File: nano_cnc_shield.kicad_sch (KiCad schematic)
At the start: 8 parts, among them Q1 IRFZ44N, U1 L7805

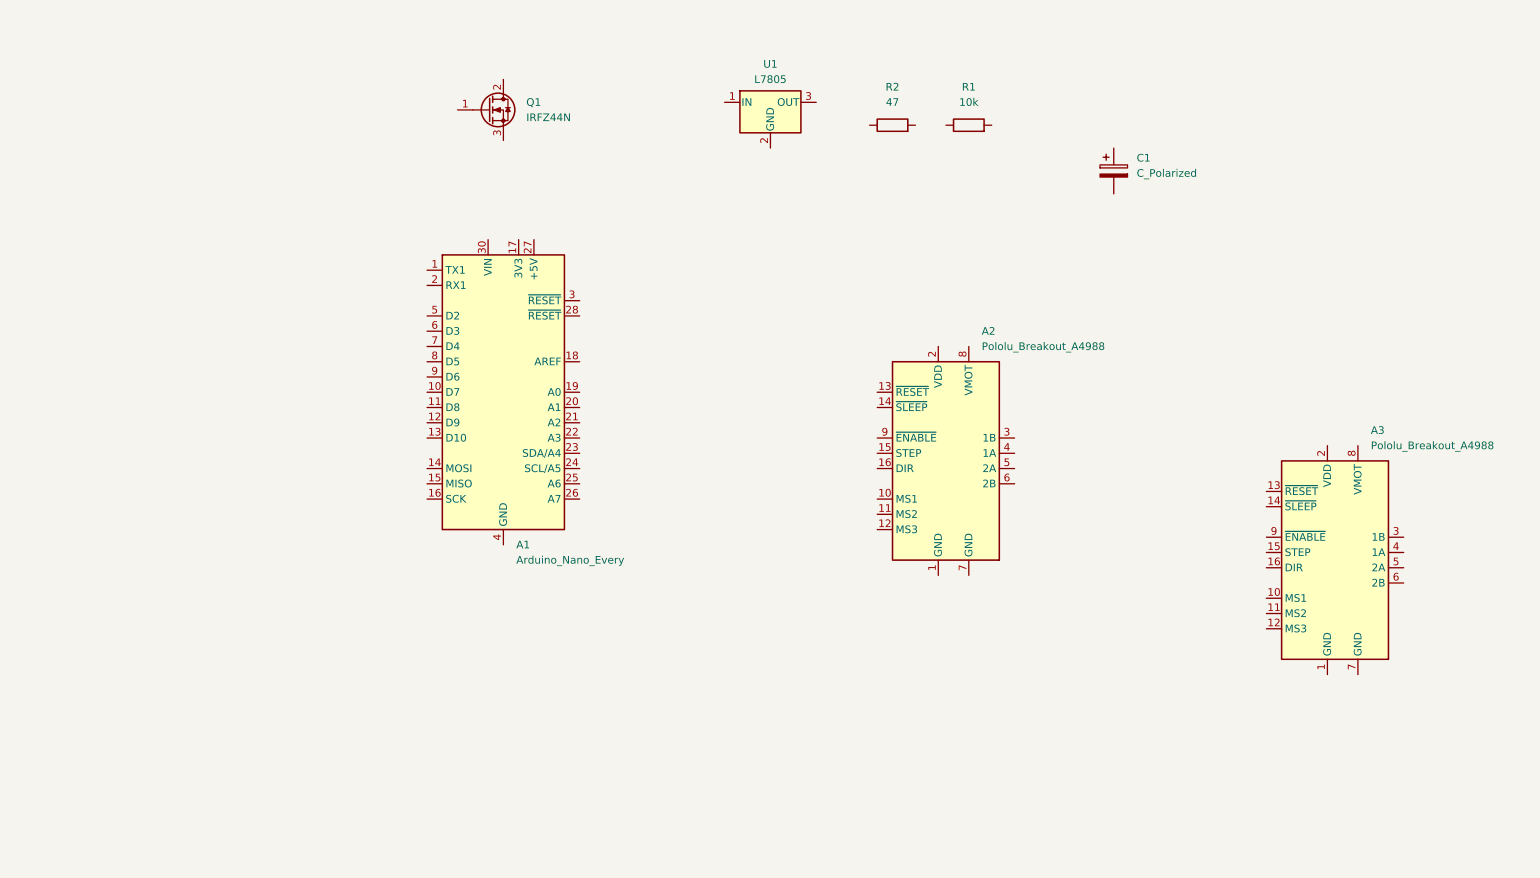
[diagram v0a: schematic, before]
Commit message: add complimentary components
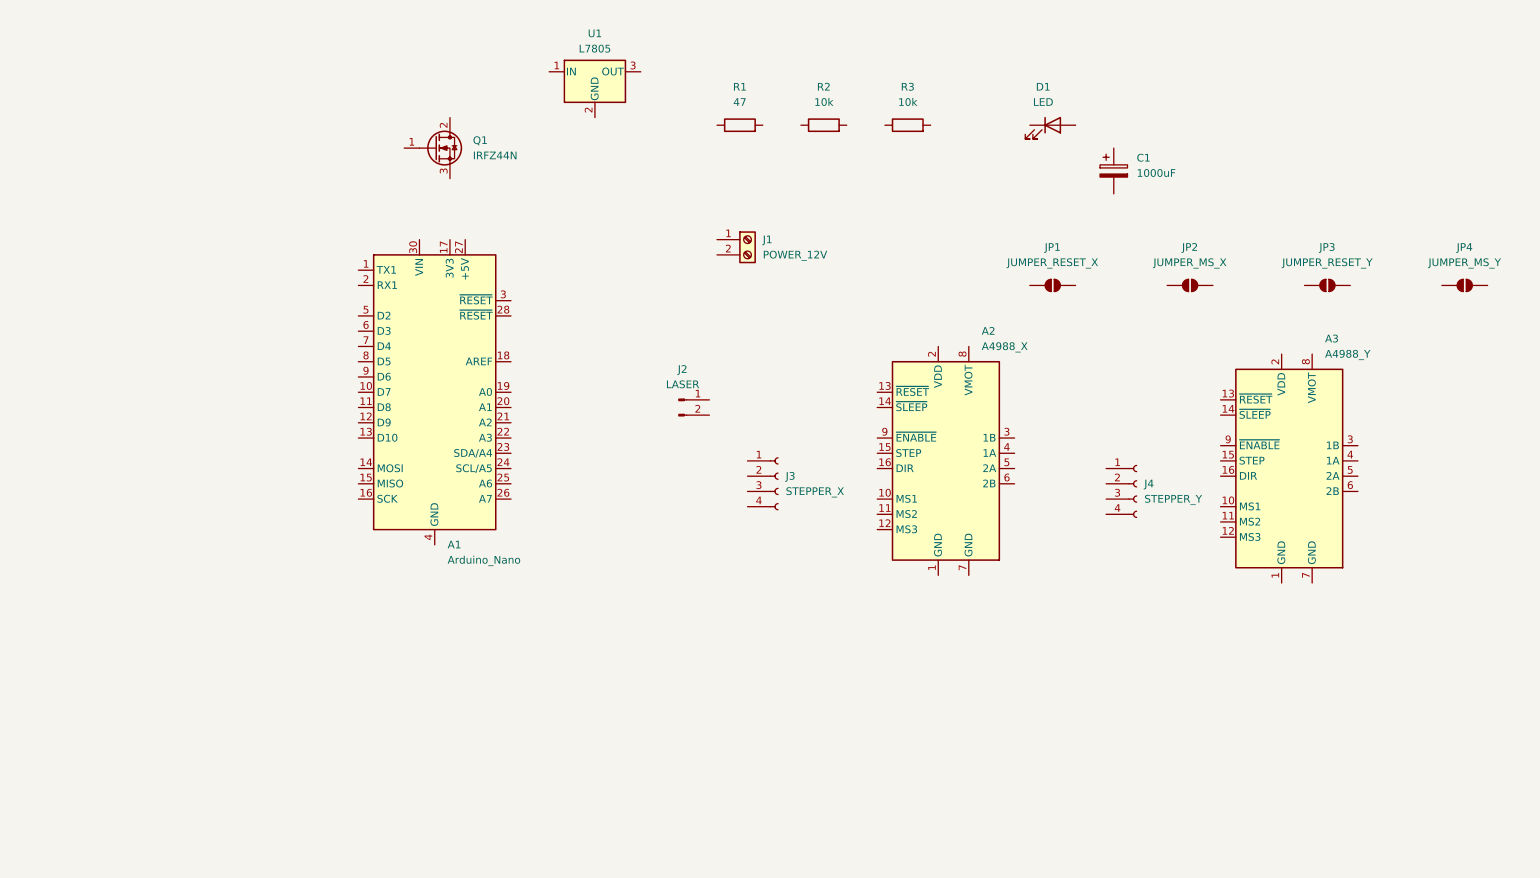
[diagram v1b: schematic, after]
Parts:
- added D1: LED, LED_THT:LED_D3.0mm, symbol Device:LED
- added J1: POWER_12V, TerminalBlock_RND:TerminalBlock_RND_205-00045_1x02_P5.00mm_Horizontal, symbol Connector:Screw_Terminal_01x02
- added J2: LASER, Connector_PinSocket_2.54mm:PinSocket_1x02_P2.54mm_Vertical, symbol Connector:Conn_01x02_Pin
- added J3: STEPPER_X, Connector_PinSocket_2.54mm:PinSocket_1x04_P2.54mm_Vertical, symbol Connector:Conn_01x04_Socket
- added J4: STEPPER_Y, Connector_PinSocket_2.54mm:PinSocket_1x04_P2.54mm_Vertical, symbol Connector:Conn_01x04_Socket
- added JP1: JUMPER_RESET_X, Jumper:SolderJumper-2_P1.3mm_Open_Pad1.0x1.5mm, symbol Jumper:SolderJumper_2_Open
- added JP2: JUMPER_MS_X, Jumper:SolderJumper-2_P1.3mm_Open_Pad1.0x1.5mm, symbol Jumper:SolderJumper_2_Open
- added JP3: JUMPER_RESET_Y, Jumper:SolderJumper-2_P1.3mm_Open_Pad1.0x1.5mm, symbol Jumper:SolderJumper_2_Open
- added JP4: JUMPER_MS_Y, Jumper:SolderJumper-2_P1.3mm_Open_Pad1.0x1.5mm, symbol Jumper:SolderJumper_2_Open
- added R3: 10k, Resistor_THT:R_Axial_DIN0207_L6.3mm_D2.5mm_P10.16mm_Horizontal, symbol Device:R
- A1: value Arduino_Nano_Every -> Arduino_Nano
- A2: value Pololu_Breakout_A4988 -> A4988_X
- A3: value Pololu_Breakout_A4988 -> A4988_Y
- C1: value C_Polarized -> 1000uF
- R1: renamed from R2; footprint (none) -> Resistor_THT:R_Axial_DIN0207_L6.3mm_D2.5mm_P10.16mm_Horizontal
- R2: renamed from R1; footprint (none) -> Resistor_THT:R_Axial_DIN0207_L6.3mm_D2.5mm_P10.16mm_Horizontal
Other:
- moved on the sheet: A1, A3, Q1, R1, R2, U1

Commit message: finished schematic
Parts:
- added SW1: POWER_SWITCH, switch:SW_Slide-03_SS22T35_8.4x3.8x6.8_P2.54mm, symbol Switch:SW_SPDT
- JP2: value JUMPER_MS_X -> JUMPER_EN_X
- JP4: value JUMPER_MS_Y -> JUMPER_EN_Y
- R3: value 10k -> 1k
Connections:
- net LASER_SIGNAL: now reaches A1.14 (MOSI)
- net LASER_SIGNAL: now also R1.1
- net +5V: now reaches A1.27 (+5V)
- net +5V: now also A2.10 (MS1), A2.11 (MS2), A2.12 (MS3), A2.2 (VDD), A3.10 (MS1), A3.11 (MS2), A3.12 (MS3), A3.2 (VDD), JP1.1 (A), JP3.1 (A)
- net GND: now reaches A1.29 (GND), A1.4 (GND)
- net GND: now also A2.1 (GND), A2.7 (GND), A3.1 (GND), A3.7 (GND), C1.2, D1.1 (K), J1.2 (GND), JP2.1 (A), JP4.1 (A), Q1.3 (S), R2.1, U1.2 (GND)
- net X_STEP: now reaches A1.5 (D2)
- net X_STEP: now also A2.15 (STEP)
- net Y_STEP: now reaches A1.6 (D3)
- net Y_STEP: now also A3.15 (STEP)
- net X_DIR: now reaches A1.8 (D5)
- net X_DIR: now also A2.16 (DIR)
- net Y_DIR: now reaches A1.9 (D6)
- net Y_DIR: now also A3.16 (DIR)
- net at R2.2: now also Q1.1 (G), R1.2
- net at C1.1: now also J1.1 (V+), SW1.2 (B)
- net at JP3.2 (B): now also A3.13 (~{RESET}), A3.14 (~{SLEEP})
- net at J3.1 (Pin_1): now also A2.3 (1B)
- net at J3.2 (Pin_2): now also A2.4 (1A)
- net at J3.3 (Pin_3): now also A2.5 (2A)
- net at J3.4 (Pin_4): now also A2.6 (2B)
- net at A2.13 (~{RESET}): now also A2.14 (~{SLEEP}), JP1.2 (B)
- net +12V: now reaches A2.8 (VMOT)
- net +12V: now also A3.8 (VMOT), U1.1 (IN), SW1.3 (C)
- net at A2.9 (~{ENABLE}): now also JP2.2 (B)
- net at R3.1: now also J2.2 (Pin_2), U1.3 (OUT)
- net at R3.2: now also D1.2 (A)
- net at A3.3 (1B): now also J4.1 (Pin_1)
- net at A3.4 (1A): now also J4.2 (Pin_2)
- net at A3.5 (2A): now also J4.3 (Pin_3)
- net at A3.6 (2B): now also J4.4 (Pin_4)
- net at A3.9 (~{ENABLE}): now also JP4.2 (B)
- net at J2.1 (Pin_1): now also Q1.2 (D)
- no-connect marks 0 -> 21
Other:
- moved on the sheet: A1, A2, A3, C1, D1, J1, J2, J3, J4, JP1, JP2, JP3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

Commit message: add general routing
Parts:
- added C2, C3: 100uF, Capacitor_THT:CP_Radial_D8.0mm_P3.50mm, symbol Device:C_Polarized
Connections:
- net +12V: now also C2.1, C3.1
- net GND: now also C2.2, C3.2

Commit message: final layout
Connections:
- no-connect marks 21 -> 23
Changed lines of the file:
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@@
+	)
+	(no_connect
+		(at 48.26 115.57)
 	)
 	(no_connect
@@
 	)
 	(no_connect
+		(at 53.34 115.57)
+	)
+	(no_connect
